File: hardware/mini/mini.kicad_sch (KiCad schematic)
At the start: 9 parts, among them J1 Conn_01x03, J2 Conn_02x05_Odd_Even, J3 Conn_02x05_Odd_Even

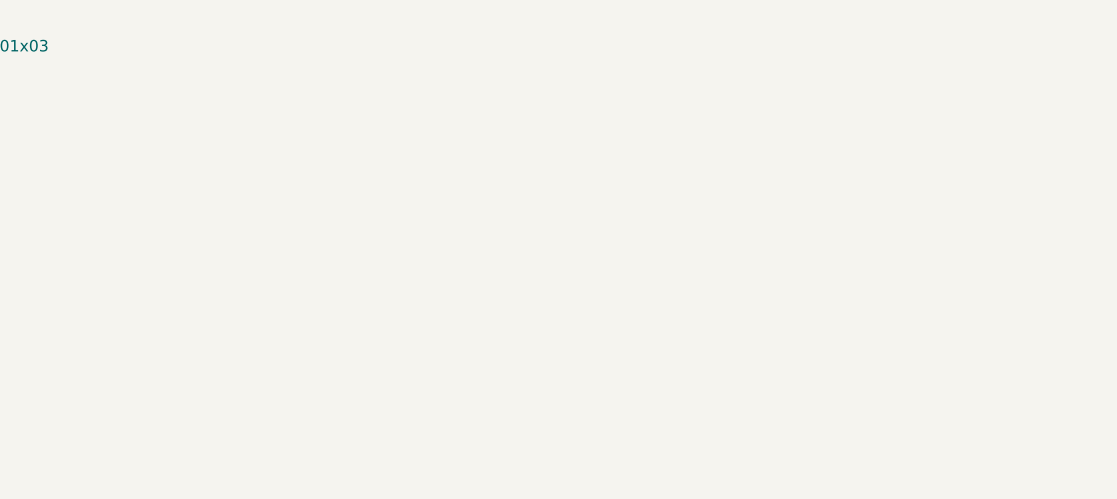
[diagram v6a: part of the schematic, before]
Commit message: finalize routing
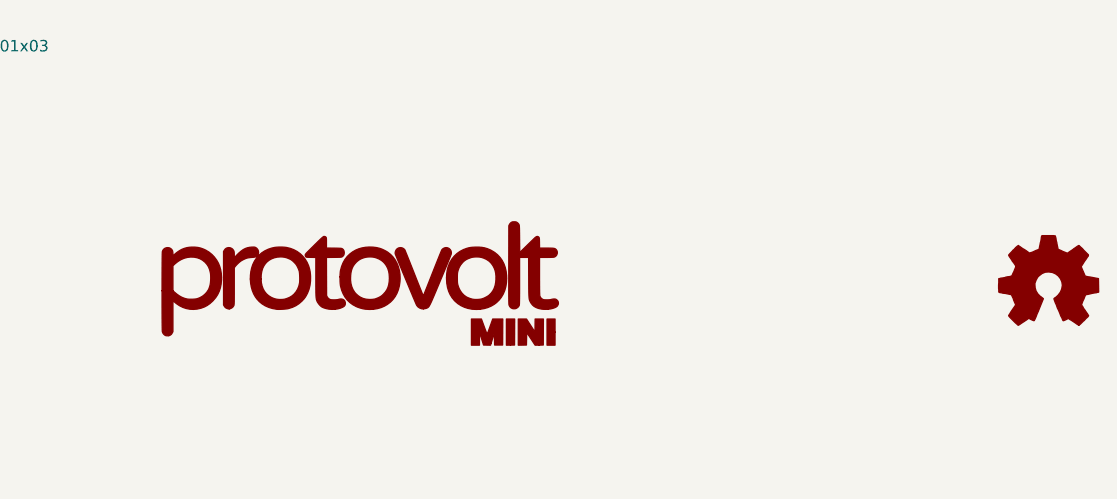
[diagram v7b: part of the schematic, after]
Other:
- title: (none) -> Protovolt MINI
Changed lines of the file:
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@@
 	(generator_version "9.0")
 	(paper "A4")
+	(title_block
+		(title "Protovolt MINI")
+		(date "2025-06-16")
+		(rev "A")
+	)
 	(text "ADDR: 0x41"
 		(exclude_from_sim no)
@@
 	)
 	(symbol
+		(lib_id "Graphic:Logo_Open_Hardware_Small")
+		(at 276.86 173.99 0)
+		(unit 1)
+		(exclude_from_sim no)
+		(in_bom no)
+		(on_board no)
+		(dnp no)
+		(fields_autoplaced yes)
+		(property "Reference" "#SYM1"
+			(at 276.86 167.005 0)
+			(effects
+				(font
+					(size 1.27 1.27)
+				)
+				(hide yes)
+			)
+		)
+		(property "Value" "Logo_Open_Hardware_Small"
+			(at 276.86 179.705 0)
+			(effects
+				(font
+					(size 1.27 1.27)
+				)
+				(hide yes)
+			)
+		)
+		(property "Footprint" ""
+			(at 276.86 173.99 0)
+			(effects
+				(font
+					(size 1.27 1.27)
+				)
+				(hide yes)
+			)
+		)
+		(property "Datasheet" "~"
+			(at 276.86 173.99 0)
+			(effects
+				(font
+					(size 1.27 1.27)
+				)
+				(hide yes)
+			)
+		)
+		(property "Description" "Open Hardware logo, small"
+			(at 276.86 173.99 0)
+			(effects
+				(font
+					(size 1.27 1.27)
+				)
+				(hide yes)
+			)
+		)
+		(property "Sim.Enable" "0"
+			(at 276.86 173.99 0)
+			(effects
+				(font
+					(size 1.27 1.27)
+				)
+				(hide yes)
+			)
+		)
+		(instances
+			(project ""
+				(path "/5aaaac9a-5acd-4aef-ad51-a6d04aa88705"
+					(reference "#SYM1")
+					(unit 1)
+				)
+			)
+		)
+	)
+	(symbol
 		(lib_id "Connector_Generic:Conn_02x05_Odd_Even")
 		(at 224.79 100.33 0)
@@
 					(unit 1)
 				)
+			)
+		)
+	)
+	(symbol
+		(lib_id "protovolt_mini:protovolt_logo")
+		(at 200.66 173.99 0)
+		(unit 1)
+		(exclude_from_sim no)
+		(in_bom yes)
+		(on_board yes)
+		(dnp no)
+		(fields_autoplaced yes)
+		(property "Reference" "#G1"
+			(at 200.66 167.261 0)
+			(effects
+				(font
+					(size 1.27 1.27)
+				)
+				(hide yes)
+			)
+		)
+		(property "Value" "protovolt_logo"
+			(at 200.66 180.719 0)
+			(effects
+				(font
+					(size 1.27 1.27)
+				)
+				(hide yes)
+			)
+		)
+		(property "Footprint" "protovolt_mini_fp:protovolt_logo"
+			(at 200.66 173.99 0)
+			(effects
+				(font
+					(size 1.27 1.27)
+				)
+				(hide yes)
+			)
+		)
+		(property "Datasheet" ""
+			(at 200.66 173.99 0)
+			(effects
+				(font
+					(size 1.27 1.27)
+				)
+				(hide yes)
+			)
+		)
+		(property "Description" ""
+			(at 200.66 173.99 0)
+			(effects
+				(font
+					(size 1.27 1.27)
+				)
+				(hide yes)
+			)
+		)
+		(instances
+			(project ""
+				(path "/5aaaac9a-5acd-4aef-ad51-a6d04aa88705"
+					(reference "#G1")
+					(unit 1)
+				)
